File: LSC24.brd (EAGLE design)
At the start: 275 x 50 mm, 123 parts, among them IC1 MCP23017SO, IC2 MCP23017SO, IC3 MCP23017SO, IC4 MCP23017SO, IC5 MCP23017SO, IC6 MCP23017SO, J1 RJ45-X8, J2 RJ45-X8, J3 RJ45-X8, J5 M06-PIN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

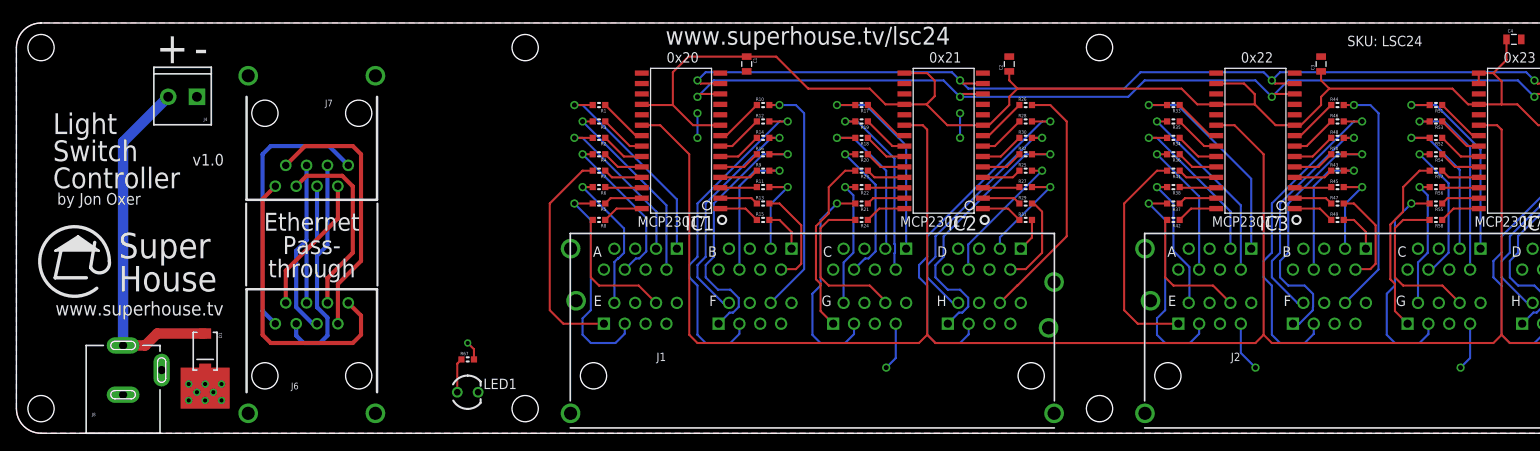
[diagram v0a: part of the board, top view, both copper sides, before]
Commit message: Routing and silkscreen for Ethernet pass-through and external power
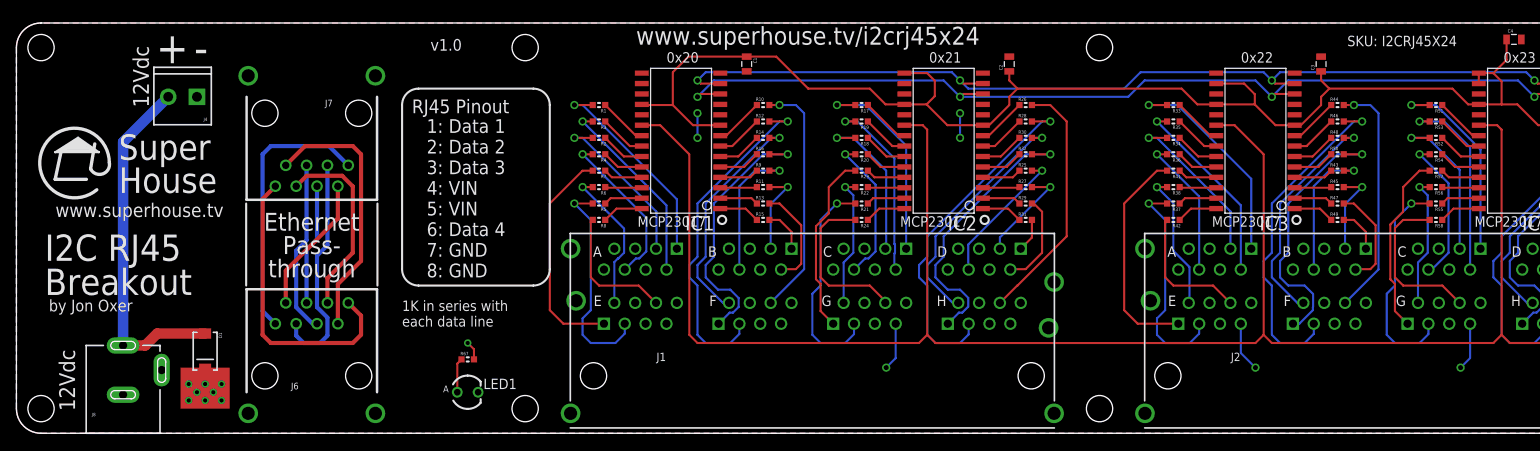
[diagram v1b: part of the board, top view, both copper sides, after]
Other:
- board text added: "12Vdc"
- board text added: "1: Data 1 2: Data 2 3: Data 3 4: VIN 5: VIN 6: Data 4 7: GND 8: GND"
- board text added: "1K in series with each data line"
- board text added: "A"
- board text added: "I2C RJ45 Breakout"
- board text added: "RJ45 Pinout"
- board text added: "SKU: I2CRJ45X24"
- board text added: "www.superhouse.tv/i2crj45x24"
- board text removed: "Light Switch Controller"
- board text removed: "SKU: LSC24"
- board text removed: "www.superhouse.tv/lsc24"
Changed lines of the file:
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@@
 <wire x1="275" y1="3" x2="272" y2="0" width="0" layer="20" curve="-90"/>
 <wire x1="272" y1="0" x2="3" y2="0" width="0" layer="20"/>
-<text x="21.453" y="32.623" size="1.4224" layer="21" font="vector" ratio="17">v1.0</text>
-<text x="96.455" y="47.354" size="2.1844" layer="21" font="vector" ratio="17" align="bottom-center">www.superhouse.tv/lsc24</text>
-<text x="162.191" y="47.171" size="1.27" layer="21" font="vector" ratio="17">SKU: LSC24</text>
+<text x="50.453" y="46.623" size="1.4224" layer="21" font="vector" ratio="17">v1.0</text>
+<text x="96.455" y="47.354" size="2.1844" layer="21" font="vector" ratio="17" align="bottom-center">www.superhouse.tv/i2crj45x24</text>
+<text x="162.191" y="47.171" size="1.27" layer="21" font="vector" ratio="17">SKU: I2CRJ45X24</text>
 <hole x="3" y="3" drill="3.2"/>
 <hole x="202" y="3" drill="3.2"/>
@@
 <text x="151.191" y="45.171" size="1.27" layer="21" font="vector" ratio="17" align="bottom-center">0x22</text>
 <text x="183.191" y="45.171" size="1.27" layer="21" font="vector" ratio="17" align="bottom-center">0x23</text>
-<wire x1="11.326" y1="20.978" x2="9.802" y2="17.676" width="0.4064" layer="21" curve="309.2564"/>
-<wire x1="11.326" y1="20.978" x2="9.04" y2="20.216" width="0.4064" layer="21" curve="-163.361194"/>
-<wire x1="9.04" y1="20.216" x2="9.548" y2="23.264" width="0.4064" layer="21"/>
-<wire x1="8.532" y1="18.946" x2="4.722" y2="18.946" width="0.4064" layer="21"/>
-<wire x1="4.722" y1="18.946" x2="5.484" y2="22.502" width="0.4064" layer="21"/>
-<wire x1="10.056" y1="22.248" x2="4.722" y2="22.248" width="0.254" layer="21"/>
-<wire x1="4.722" y1="22.248" x2="7.516" y2="24.026" width="0.254" layer="21"/>
-<wire x1="7.516" y1="24.026" x2="10.056" y2="22.248" width="0.254" layer="21"/>
-<wire x1="5.23" y1="22.502" x2="5.484" y2="22.502" width="0.254" layer="21"/>
-<wire x1="5.484" y1="22.502" x2="9.294" y2="22.502" width="0.254" layer="21"/>
-<wire x1="9.294" y1="22.502" x2="7.516" y2="23.772" width="0.254" layer="21"/>
-<wire x1="7.516" y1="23.772" x2="5.484" y2="22.502" width="0.254" layer="21"/>
-<wire x1="8.786" y1="22.756" x2="5.992" y2="22.756" width="0.4064" layer="21"/>
-<wire x1="5.992" y1="22.756" x2="7.516" y2="23.518" width="0.4064" layer="21"/>
-<wire x1="7.516" y1="23.518" x2="8.278" y2="23.01" width="0.4064" layer="21"/>
-<wire x1="8.278" y1="23.01" x2="7.008" y2="23.01" width="0.4064" layer="21"/>
-<wire x1="7.008" y1="23.01" x2="7.516" y2="23.264" width="0.4064" layer="21"/>
-<text x="12.455" y="20.854" size="3.1" layer="21" font="vector" ratio="17" distance="30" align="center-left">Super
+<wire x1="11.326" y1="32.978" x2="9.802" y2="29.676" width="0.4064" layer="21" curve="309.2564"/>
+<wire x1="11.326" y1="32.978" x2="9.04" y2="32.216" width="0.4064" layer="21" curve="-163.361194"/>
+<wire x1="9.04" y1="32.216" x2="9.548" y2="35.264" width="0.4064" layer="21"/>
+<wire x1="8.532" y1="30.946" x2="4.722" y2="30.946" width="0.4064" layer="21"/>
+<wire x1="4.722" y1="30.946" x2="5.484" y2="34.502" width="0.4064" layer="21"/>
+<wire x1="10.056" y1="34.248" x2="4.722" y2="34.248" width="0.254" layer="21"/>
+<wire x1="4.722" y1="34.248" x2="7.516" y2="36.026" width="0.254" layer="21"/>
+<wire x1="7.516" y1="36.026" x2="10.056" y2="34.248" width="0.254" layer="21"/>
+<wire x1="5.23" y1="34.502" x2="5.484" y2="34.502" width="0.254" layer="21"/>
+<wire x1="5.484" y1="34.502" x2="9.294" y2="34.502" width="0.254" layer="21"/>
+<wire x1="9.294" y1="34.502" x2="7.516" y2="35.772" width="0.254" layer="21"/>
+<wire x1="7.516" y1="35.772" x2="5.484" y2="34.502" width="0.254" layer="21"/>
+<wire x1="8.786" y1="34.756" x2="5.992" y2="34.756" width="0.4064" layer="21"/>
+<wire x1="5.992" y1="34.756" x2="7.516" y2="35.518" width="0.4064" layer="21"/>
+<wire x1="7.516" y1="35.518" x2="8.278" y2="35.01" width="0.4064" layer="21"/>
+<wire x1="8.278" y1="35.01" x2="7.008" y2="35.01" width="0.4064" layer="21"/>
+<wire x1="7.008" y1="35.01" x2="7.516" y2="35.264" width="0.4064" layer="21"/>
+<text x="12.455" y="32.854" size="3.1" layer="21" font="vector" ratio="17" distance="30" align="center-left">Super
 House</text>
-<text x="4.455" y="29.854" size="2.54" layer="21" font="vector" ratio="17" distance="30">Light
-Switch
-Controller</text>
-<text x="4.955" y="27.854" size="1.4224" layer="21" font="vector" ratio="17" distance="30">by Jon Oxer</text>
+<text x="3.455" y="16.854" size="3.2" layer="21" font="vector" ratio="17" distance="30">I2C RJ45
+Breakout</text>
+<text x="3.955" y="14.854" size="1.4224" layer="21" font="vector" ratio="17" distance="30">by Jon Oxer</text>
 <text x="193.455" y="34.854" size="1.6764" layer="22" font="vector" ratio="17" distance="30" rot="MR0">Copyright 2019 SuperHouse Automation Pty Ltd
 Released under the terms
@@
 Pass-
 through</text>
-<text x="15" y="14.354" size="1.6764" layer="21" font="vector" ratio="17" align="bottom-center">www.superhouse.tv</text>
+<text x="15" y="26.354" size="1.6764" layer="21" font="vector" ratio="17" align="bottom-center">www.superhouse.tv</text>
 <dimension x1="3" y1="51" x2="62" y2="51" x3="32.5" y3="52" textsize="1.778" layer="47"/>
 <dimension x1="62" y1="51" x2="132" y2="51" x3="97" y3="52" textsize="1.778" layer="47"/>
@@
 <text x="19" y="47" size="3.81" layer="21" font="vector" ratio="16" align="center">+</text>
 <text x="22.5" y="47" size="3.81" layer="21" font="vector" ratio="16" align="center">-</text>
+<text x="52" y="5" size="0.8128" layer="21" font="vector" ratio="12">A</text>
+<text x="7.146" y="6.455" size="1.9304" layer="21" font="vector" ratio="17" distance="30" rot="R90" align="bottom-center">12Vdc</text>
+<text x="16.146" y="43.455" size="1.9304" layer="21" font="vector" ratio="17" distance="30" rot="R90" align="bottom-center">12Vdc</text>
+<text x="50" y="19" size="1.6764" layer="21" font="vector" ratio="12">1: Data 1
+2: Data 2
+3: Data 3
+4: VIN
+5: VIN
+6: Data 4
+7: GND
+8: GND</text>
+<text x="48.2" y="39" size="1.6764" layer="21" font="vector" ratio="16">RJ45 Pinout</text>
+<wire x1="49" y1="42" x2="47" y2="40" width="0.254" layer="21" curve="90"/>
+<wire x1="47" y1="40" x2="47" y2="20" width="0.254" layer="21"/>
+<wire x1="47" y1="20" x2="49" y2="18" width="0.254" layer="21" curve="90"/>
+<wire x1="49" y1="18" x2="63" y2="18" width="0.254" layer="21"/>
+<wire x1="63" y1="18" x2="65" y2="20" width="0.254" layer="21" curve="90"/>
+<wire x1="65" y1="20" x2="65" y2="40" width="0.254" layer="21"/>
+<wire x1="65" y1="40" x2="63" y2="42" width="0.254" layer="21" curve="90"/>
+<wire x1="63" y1="42" x2="49" y2="42" width="0.254" layer="21"/>
+<text x="47" y="13" size="1.27" layer="21" font="vector" ratio="12">1K in series with
+each data line</text>
 </plain>
 <attributes>
